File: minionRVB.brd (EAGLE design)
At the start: 160 x 100 mm, 106 parts

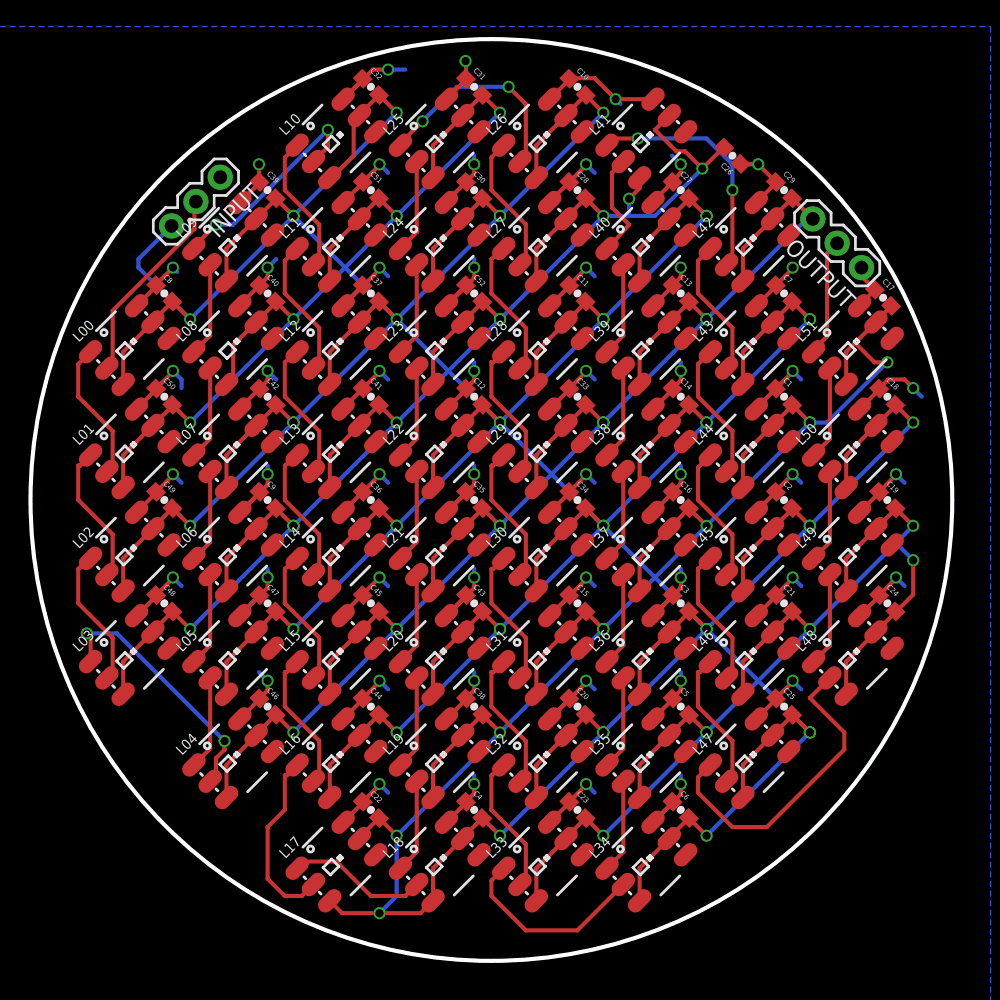
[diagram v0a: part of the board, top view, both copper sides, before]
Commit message: Bigger +5v
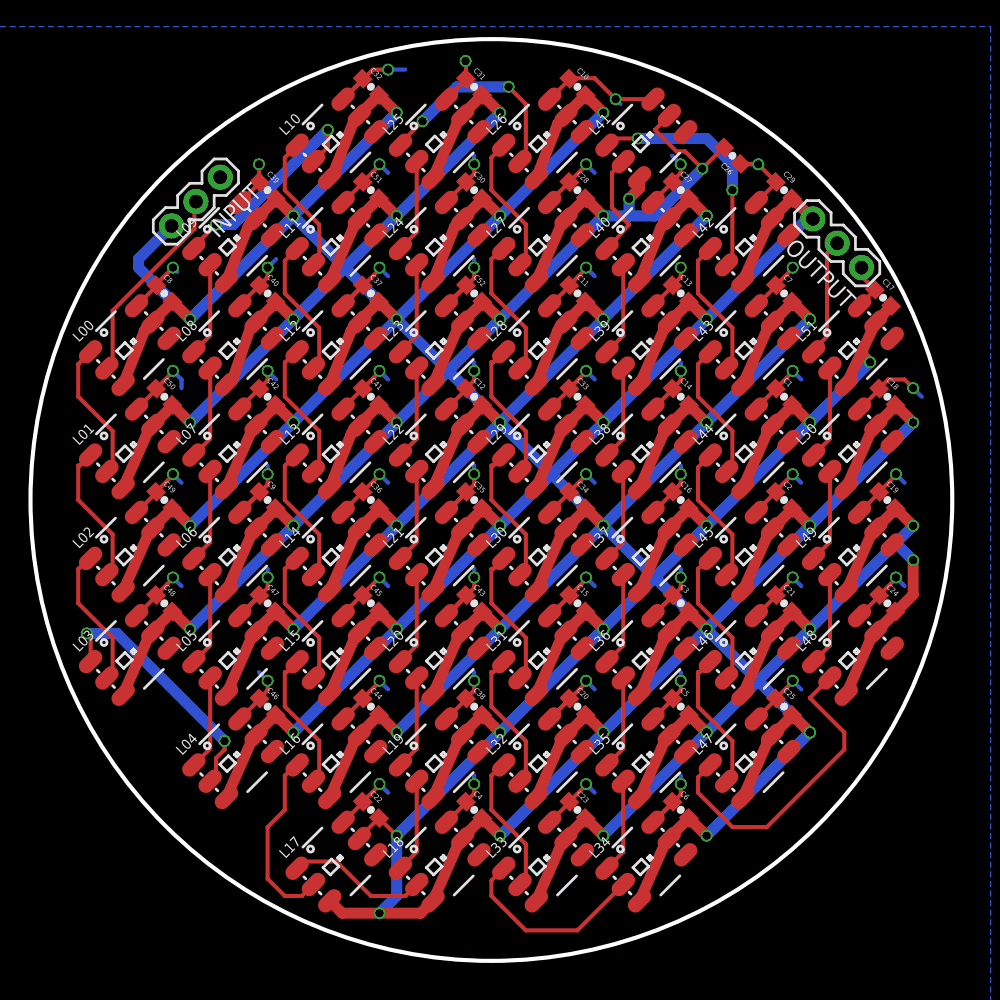
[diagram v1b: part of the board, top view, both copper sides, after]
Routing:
- net VCC: track 998.5 -> 976.0 mm

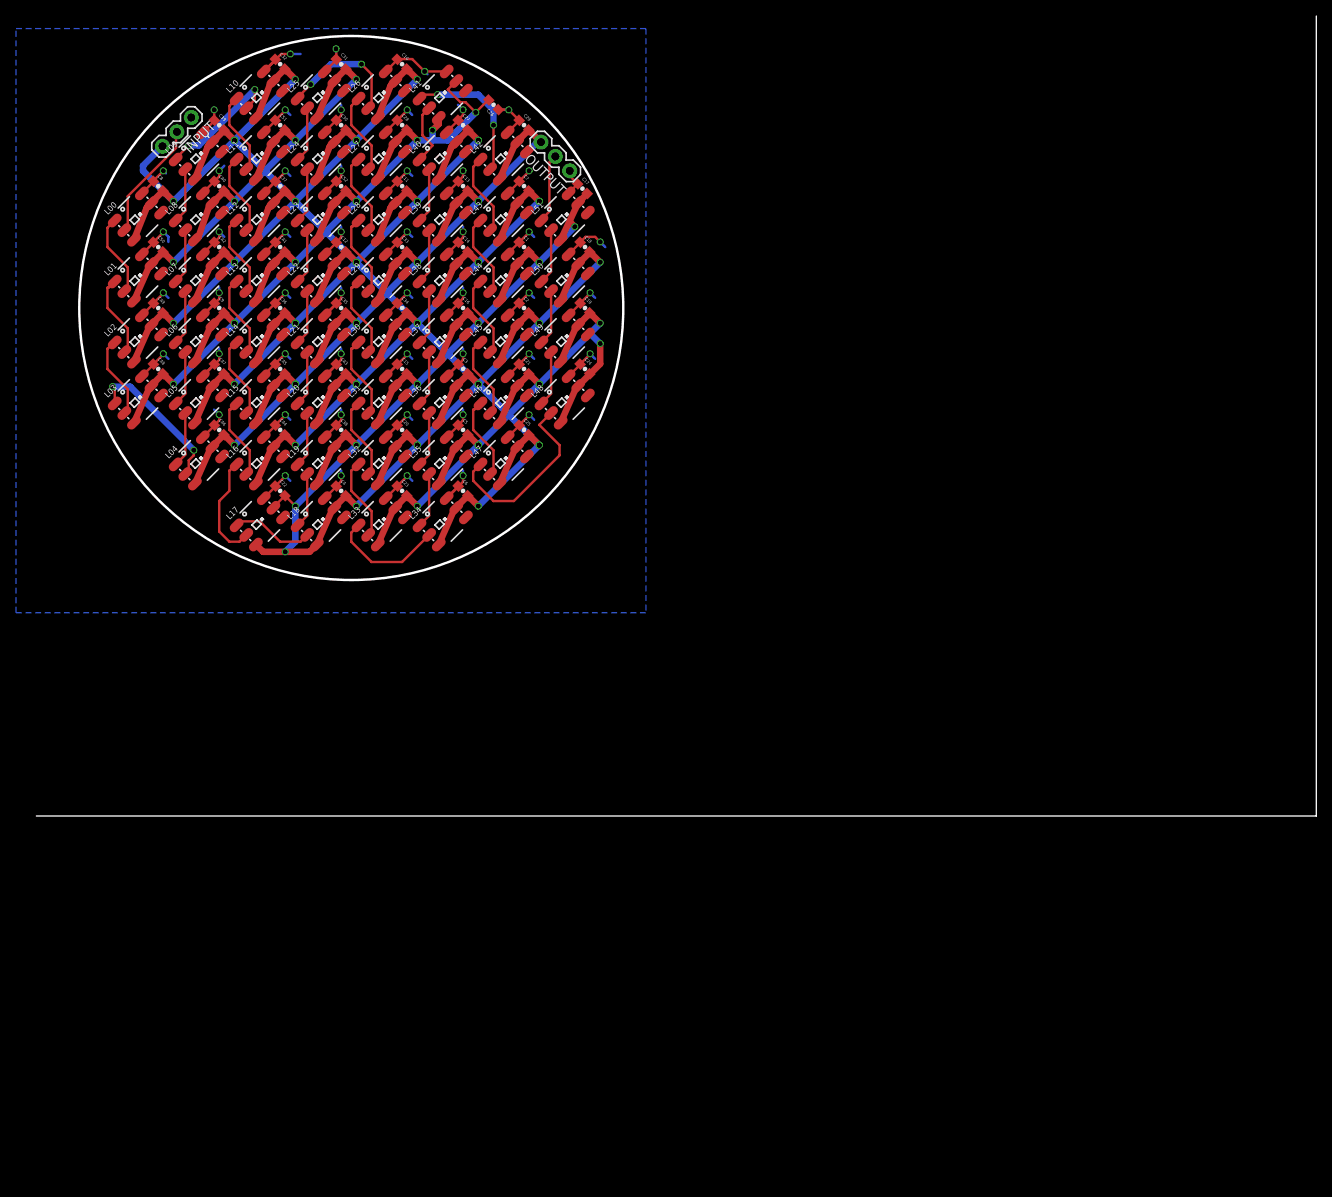
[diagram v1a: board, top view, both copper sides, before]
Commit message: Add a teensy adaptor v1
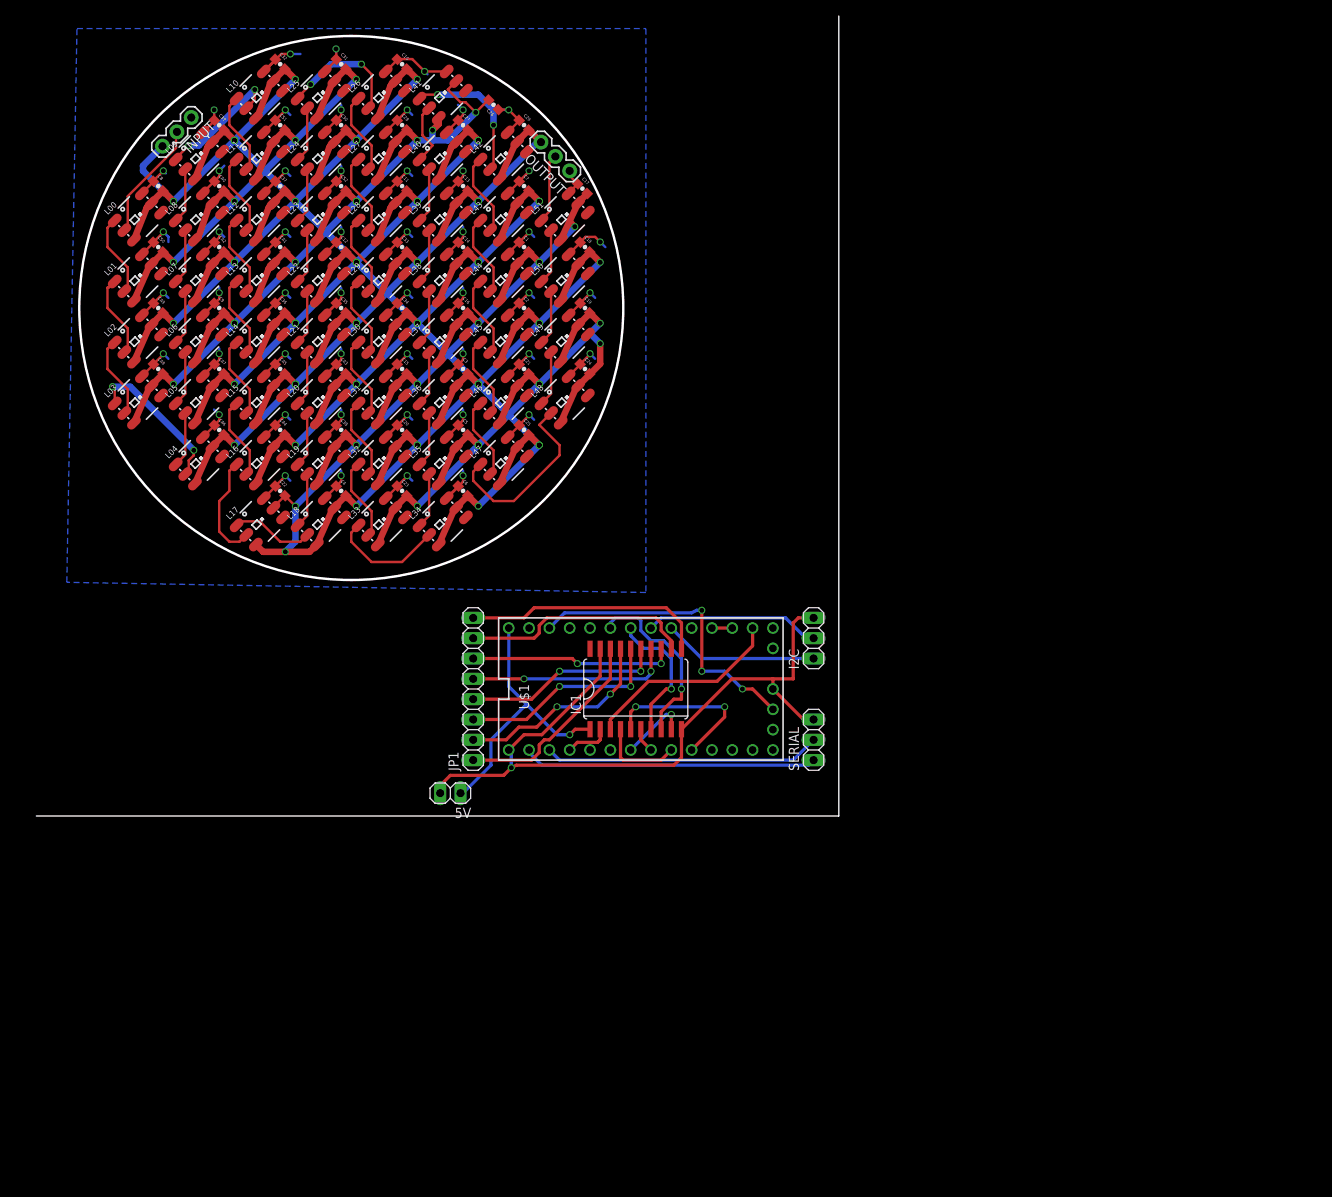
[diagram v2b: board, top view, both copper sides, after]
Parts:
- added 5V: (no value), pinhead:1X02
- added I2C, SERIAL: (no value), pinhead:1X03
- added IC1: 74HCT245DW, 74xx-eu:SO20W
- added JP1: (no value), pinhead:1X08
- added U$1: TEENSY_3.0_BASIC-PGM, Teensy3.0:TEENSY_3.0_BASIC-PGM
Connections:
- new net 3.3V: U$1.3.3V, U$1.3.3V1
- new net 5V: 5V.1, IC1.1, U$1.VIN
- new net AGND: U$1.AGND
- new net FRAMESYNC: U$1.12
- new net N$1: U$1.15/A1, U$1.16/A2
- new net N$42: IC1.18, JP1.1
- new net N$54: IC1.17, JP1.2
- new net N$55: IC1.16, JP1.3
- new net N$56: IC1.15, JP1.4
- new net N$57: IC1.14, JP1.5
- new net N$58: IC1.13, JP1.6
- new net N$59: IC1.12, JP1.7
- new net N$60: IC1.11, JP1.8
- new net RX: SERIAL.1, U$1.0
- new net SCL0: I2C.2, U$1.19/A5
- new net SDA0: I2C.1, U$1.18/A4
- new net STRIP01: IC1.2, U$1.2
- new net STRIP02: IC1.3, U$1.14/A0
- new net STRIP03: IC1.4, U$1.7
- new net STRIP04: IC1.5, U$1.8
- new net STRIP05: IC1.6, U$1.6
- new net STRIP06: IC1.7, U$1.20/A6
- new net STRIP07: IC1.8, U$1.21/A7
- new net STRIP08: IC1.9, U$1.5
- new net TX: SERIAL.2, U$1.1
- new net VBAT: U$1.VBAT
- net GND: now also 5V.2, I2C.3, IC1.10, IC1.19, SERIAL.3, U$1.GND, U$1.GND1
- net VCC: now also IC1.20
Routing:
- net GND: track 263.5 -> 354.9 mm, vias 50 -> 51
- net 3.3V: track 0.00 -> 38.4 mm, vias 0 -> 3
- net RX: track 0.00 -> 36.8 mm
- net 5V: track 0.00 -> 35.0 mm, vias 0 -> 1
- net TX: track 0.00 -> 34.6 mm
- net N$60: track 0.00 -> 30.6 mm
- net N$59: track 0.00 -> 29.1 mm
- net N$55: track 0.00 -> 26.1 mm, vias 0 -> 2
- net N$54: track 0.00 -> 25.7 mm, vias 0 -> 2
- net N$42: track 0.00 -> 25.7 mm
- net N$58: track 0.00 -> 25.6 mm, vias 0 -> 2
- net N$57: track 0.00 -> 25.6 mm, vias 0 -> 2
- net N$56: track 0.00 -> 25.2 mm, vias 0 -> 2
- net STRIP02: track 0.00 -> 25.0 mm
- net STRIP07: track 0.00 -> 23.1 mm, vias 0 -> 1
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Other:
- board size 160 x 100 mm -> 100.3 x 100 mm

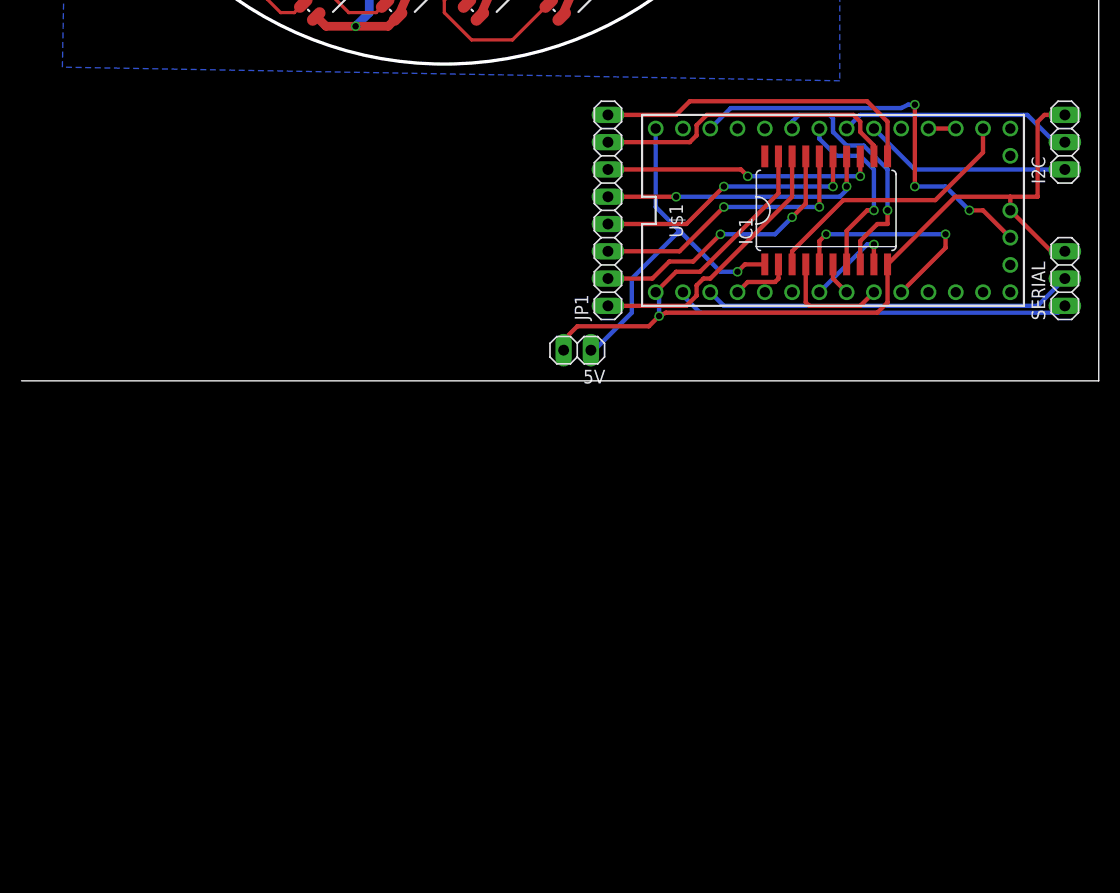
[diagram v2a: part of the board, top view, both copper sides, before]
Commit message: Teensy adaptor v2
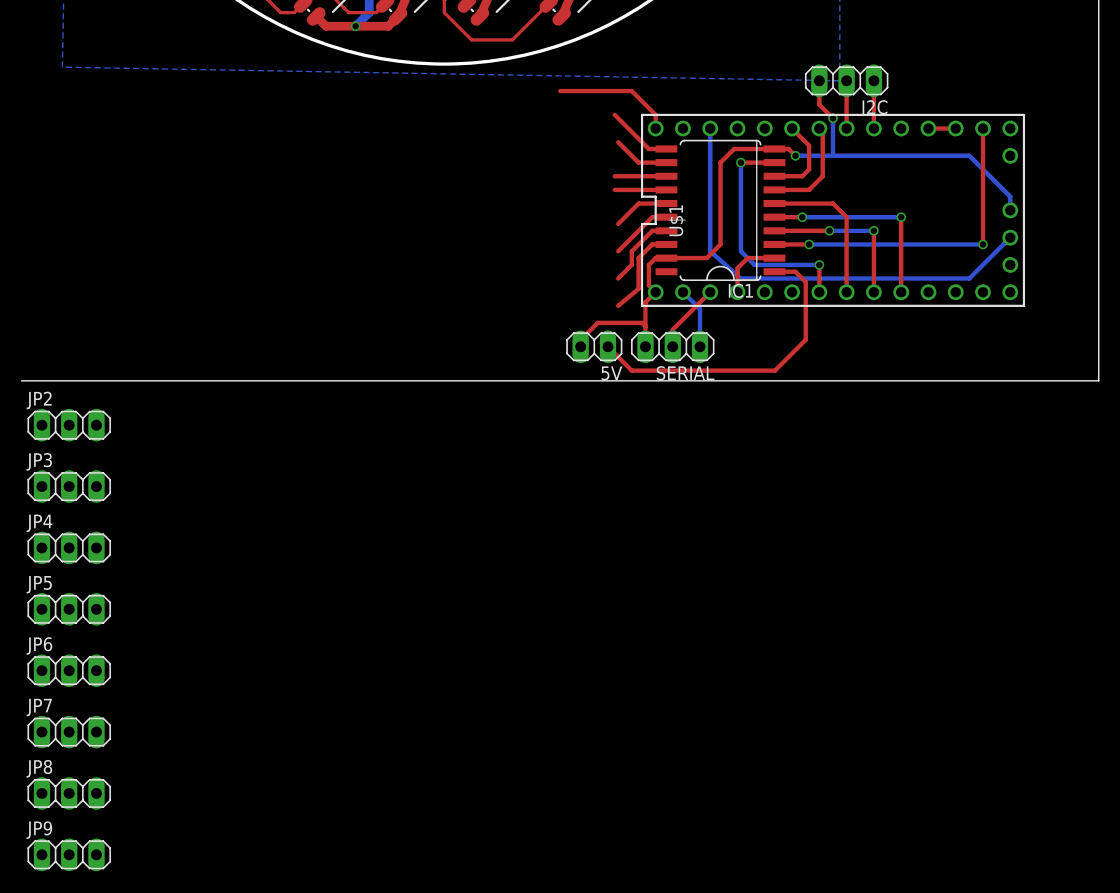
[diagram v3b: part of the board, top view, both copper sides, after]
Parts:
- removed JP1: (no value), pinhead:1X08
- added JP2, JP3, JP4, JP5, JP6, JP7, JP8, JP9: (no value), pinhead:1X03
- moved SERIAL 37.1 mm to (60.6, 3.17), turned to 180 degrees
- moved I2C 21.1 mm to (76.8, 27.9), turned to 180 degrees
- moved IC1 9.84 mm to (65.1, 15.9), turned to 90 degrees
- moved 5V 1.62 mm to (53.3, 3.17)
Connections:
- net 5V: now also JP2.3, JP3.3, JP4.3, JP5.3, JP6.3, JP7.3, JP8.3, JP9.3
- net GND: now also JP2.1, JP3.1, JP4.1, JP5.1, JP6.1, JP7.1, JP8.1, JP9.1
- net N$42: now also JP2.2; no longer JP1.1
- net N$54: now also JP3.2; no longer JP1.2
- net N$55: now also JP4.2; no longer JP1.3
- net N$56: now also JP5.2; no longer JP1.4
- net N$57: now also JP6.2; no longer JP1.5
- net N$58: now also JP7.2; no longer JP1.6
- net N$59: now also JP8.2; no longer JP1.7
- net N$60: now also JP9.2; no longer JP1.8
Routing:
- net RX: track 36.8 -> 5.74 mm
- net TX: track 34.6 -> 6.53 mm
- net N$60: track 30.6 -> 6.13 mm
- net N$59: track 29.1 -> 5.28 mm
- net GND: track 354.9 -> 332.5 mm, vias 51 -> 52
- net N$58: track 25.6 -> 4.81 mm, vias 2 -> 0
- net N$57: track 25.6 -> 4.81 mm, vias 2 -> 0
- net N$55: track 26.1 -> 5.81 mm, vias 2 -> 0
- net N$56: track 25.2 -> 5.28 mm, vias 2 -> 0
- net N$54: track 25.7 -> 7.08 mm, vias 2 -> 0
- net SCL0: track 21.9 -> 4.45 mm
- net N$42: track 25.7 -> 8.45 mm
- net STRIP07: track 23.1 -> 7.96 mm, vias 1 -> 0
- net SDA0: track 19.4 -> 4.45 mm
- net STRIP08: track 8.78 -> 21.7 mm, vias 1 -> 2
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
